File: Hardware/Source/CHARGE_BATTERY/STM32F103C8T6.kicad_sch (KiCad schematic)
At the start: 25 parts, among them J5 Conn_01x04_Pin, SW2 SW_Push, U7 STM32F103C8Tx, U8 ADS1115IDGS

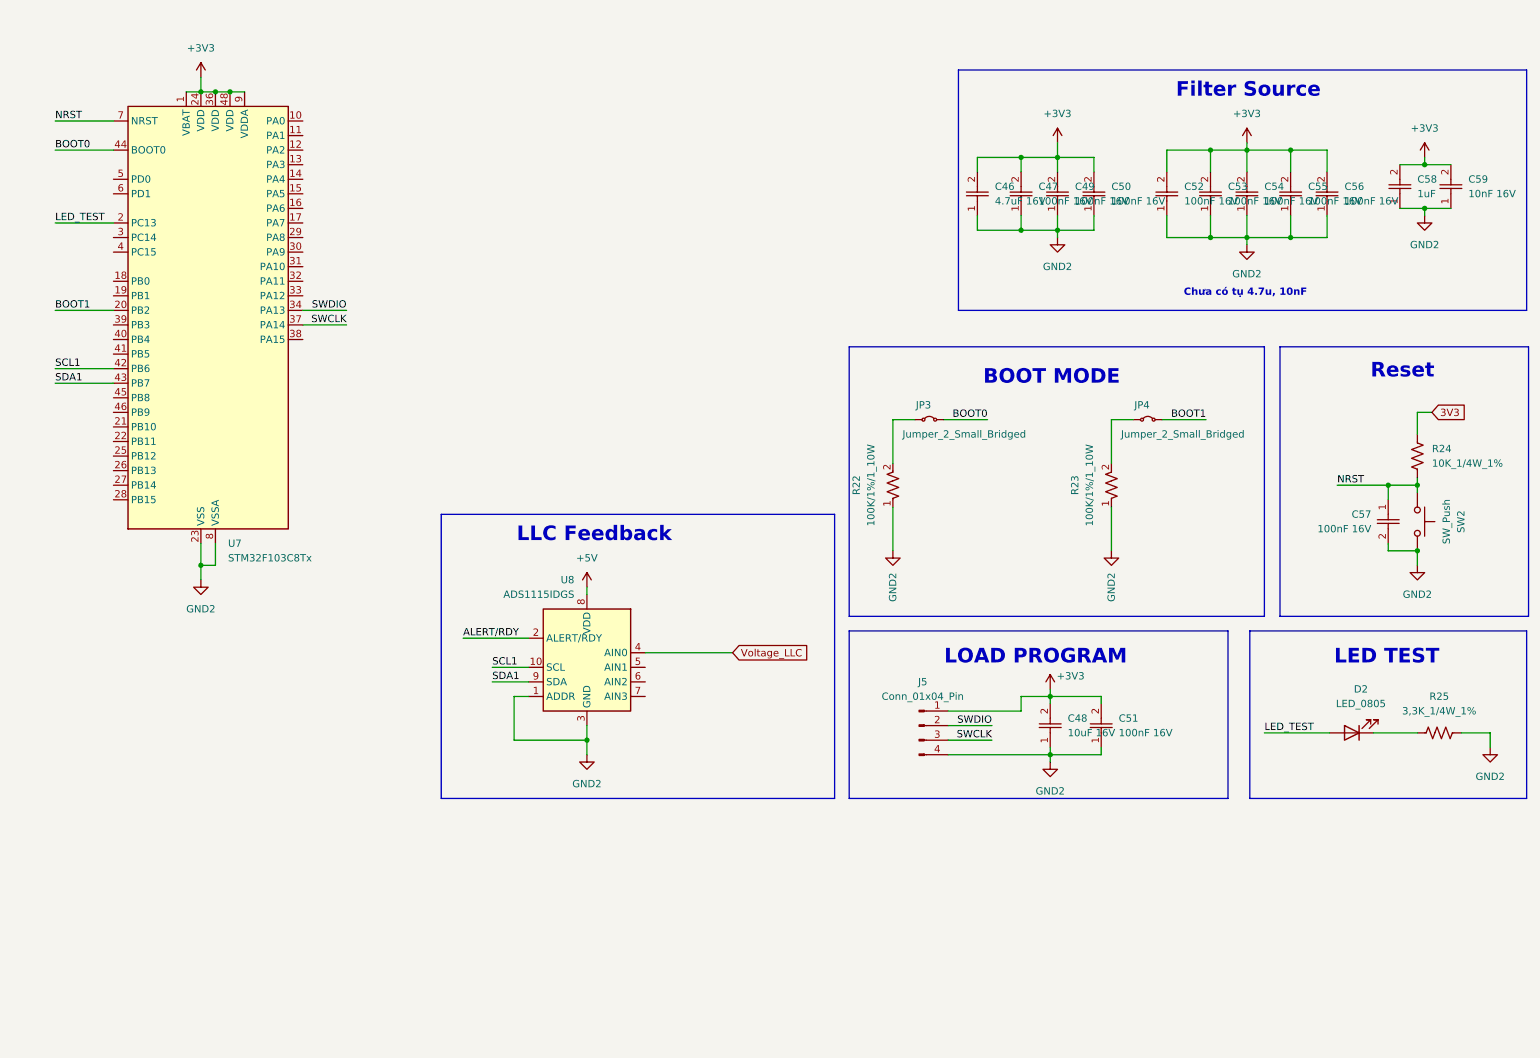
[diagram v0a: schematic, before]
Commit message: Hardware: Update PFC and Sheet Entry
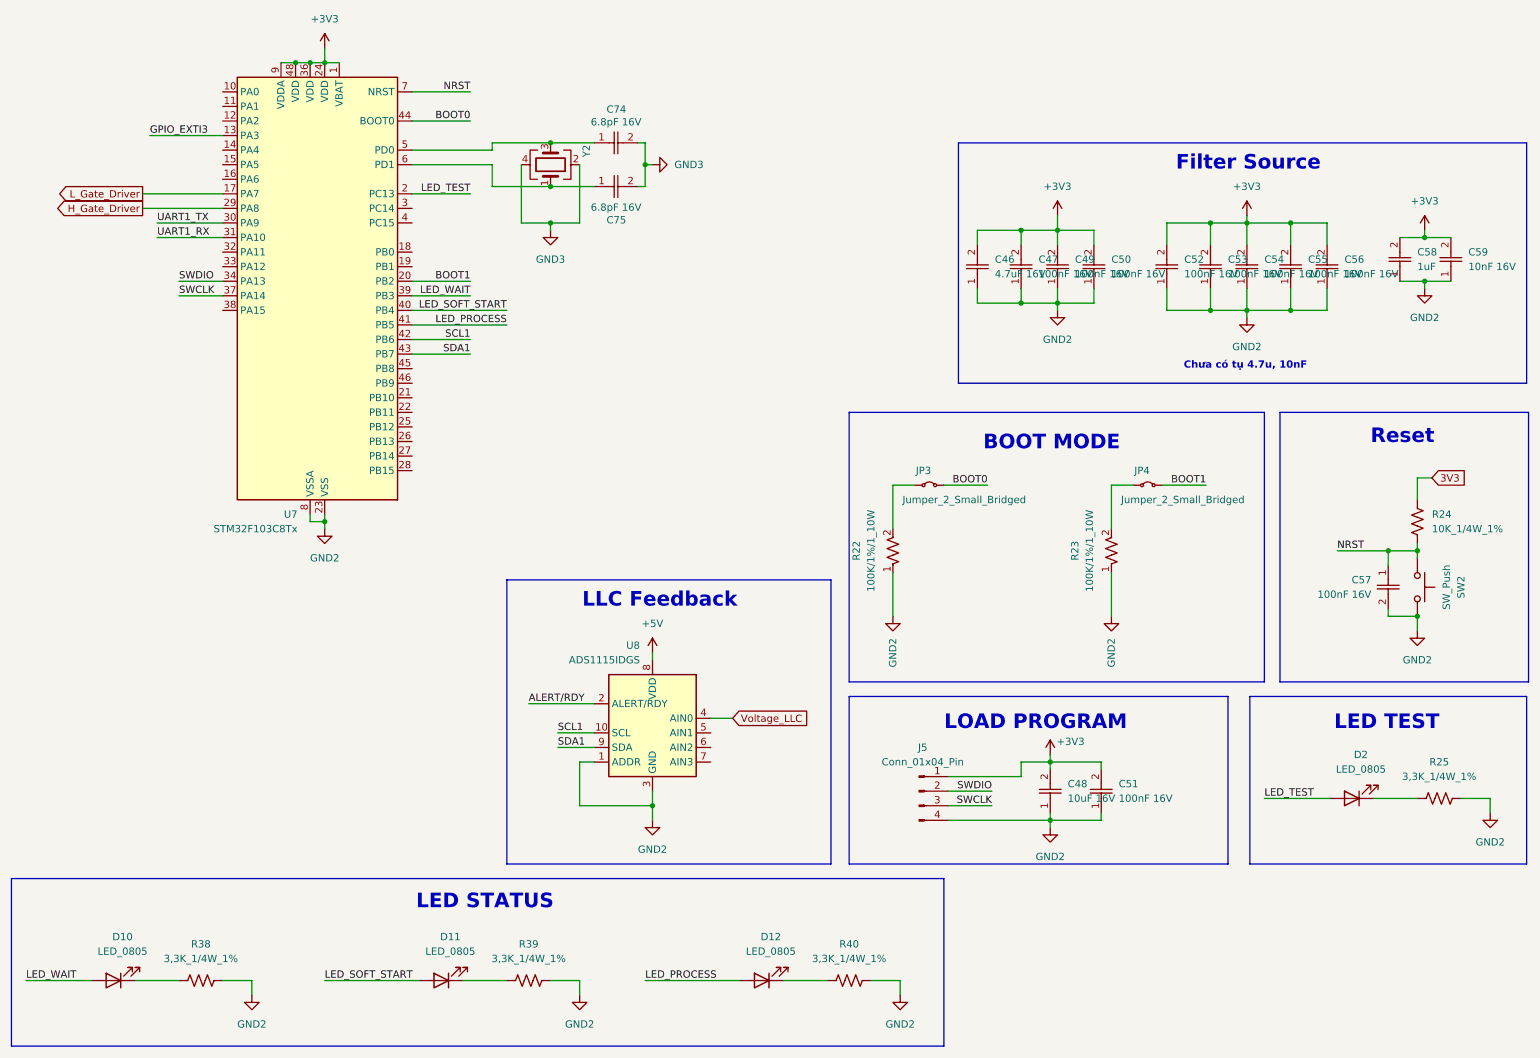
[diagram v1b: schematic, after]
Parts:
- added C74, C75: 6.8pF 16V, charge_battery_footprint_lib:C_0603_1608Metric, symbol charge_battery_sym_lib:Ceramic_Cap_SMD_100nF_16V
- added D10, D11, D12: LED_0805, charge_battery_footprint_lib:LED_0805, symbol charge_battery_sym_lib:LED_0805
- added R38, R39, R40: 3,3K_1/4W_1%, charge_battery_footprint_lib:Res_3.3R_1_4W_1, symbol charge_battery_sym_lib:Res_hole_3,3K_1/4W_1%
- added Y2: Crystal_8MHz_SMD-4PIN, charge_battery_footprint_lib:IPP65R095C7, symbol charge_battery_sym_lib:Crystal_8MHz_SMD-4PIN
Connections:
- net GND2: now also R38.2, R39.2, R40.2
- net GPIO_EXTI3: now reaches U7.13 (PA3)
- net L_Gate_Driver: now reaches U7.17 (PA7)
- net H_Gate_Driver: now reaches U7.29 (PA8)
- net UART1_TX: now reaches U7.30 (PA9)
- net UART1_RX: now reaches U7.31 (PA10)
- net LED_WAIT: now reaches U7.39 (PB3)
- net LED_WAIT: now also D10.2 (A)
- net LED_SOFT_START: now reaches U7.40 (PB4)
- net LED_SOFT_START: now also D11.2 (A)
- net LED_PROCESS: now reaches U7.41 (PB5)
- net LED_PROCESS: now also D12.2 (A)
- net at U7.5 (PD0): now also C74.1, Y2.3
- net at U7.6 (PD1): now also C75.1, Y2.1
- new net: D12.1 (K), R40.1
- new net: D11.1 (K), R39.1
- new net: D10.1 (K), R38.1
- new net GND3: C74.2, C75.2, Y2.2, Y2.4
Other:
- note added: "LED STATUS"
- moved on the sheet: C46, C47, C48, C49, C50, C51, C52, C53, C54, C55, C56, C57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
